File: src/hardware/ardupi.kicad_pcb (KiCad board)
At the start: 2 copper layers, 65 x 56 mm, 72 parts, among them J1 Conn_01x05, J2 Conn_01x06, J3 RPI-4B-Header, J4 PWM_Header, J5 Conn_01x02, J6 Conn_01x04, J7 Conn_01x04, J8 Conn_01x05, J9 Conn_01x10, M1 NEO-M8Q-01A, U1 ULN2803ADWR, U2 CAT24C32WI-GT3, U3 ADS1115IDGSR, U4 RFM95W-915S2, U5 MPU-9250, U6 PCA9685PW, U7 BMP280, U8 MPU-9250

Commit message: version bump
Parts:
- removed C_PCA1: 10uF, Capacitor_SMD:CP_Elec_8x5.4
- removed R1, R10, R5, R6, R8: 10k, Resistor_SMD:R_0402_1005Metric
- removed R16, R17, R18, R19, R20, R21, R22, R23: 220 Ω, Resistor_SMD:R_0402_1005Metric
- removed R2, R3, R4: 10K, Resistor_SMD:R_0402_1005Metric
- removed SJ1, SJ2, SJ3, SJ4, SJ5, SJ6: SolderJumper-Open_Pad, Ardupi:SolderJumper-Open_Pad
- removed U6: PCA9685PW, Ardupi:PCA9685PW
- removed U8: MPU-9250, Ardupi:MPU-9250
- J4: value PWM_Header -> Conn_01x06; footprint Ardupi:PWM_Header -> Connector_JST:JST_EH_B6B-EH-A_1x06_P2.50mm_Vertical
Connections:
- J4 pad 1: Net-(J4-Pad1) -> GND
- J4 pad 2: V_EXT -> /PCA_EN
- J4 pad 3: GND -> /SCL
- J4 pad 4: Net-(J4-Pad4) -> /SDA
- J4 pad 5: V_EXT -> +5V
- J4 pad 6: GND -> V_EXT

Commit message: update symbols
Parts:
- removed C4: 0.1uF, Capacitor_SMD:C_0402_1005Metric
- removed C6: 0.01uF, Capacitor_SMD:C_0402_1005Metric
- removed C8: 1uF, Capacitor_SMD:C_0402_1005Metric
- removed R24, R25, R31, R33, R34: 10KΩ, Resistor_SMD:R_0402_1005Metric
- removed U7: BMP280, Ardupi:BMP280
- added C12: 0.1uF, Capacitor_SMD:C_0402_1005Metric, F.Cu at (60.2, 140.2)
- added C14: 0.01uF, Capacitor_SMD:C_0402_1005Metric, F.Cu at (46.2, 153.8)
- added C15: 1uF, Capacitor_SMD:C_0402_1005Metric, F.Cu at (64.9, 134.3)
- added D1: B560C, Ardupi:B560C-13-F, F.Cu at (52.7, 137.1)
- added M2: NEO-M8Q-01A, Ardupi:NEO-M8Q-01A, F.Cu at (60.9, 118.6)
- added R1: 523k, Resistor_SMD:R_0402_1005Metric, F.Cu at (31.5, 163.7)
- added R10: 10KΩ, Resistor_SMD:R_0402_1005Metric, F.Cu at (57.3, 142.0)
- added R16: 10KΩ, Resistor_SMD:R_0402_1005Metric, F.Cu at (66.5, 128.3)
- added R17: 53.6 k, Resistor_SMD:R_0402_1005Metric, F.Cu at (47.1, 149.8)
- added R18: 10.2 k, Resistor_SMD:R_0402_1005Metric, F.Cu at (37.4, 154.0)
- added R2: 84.5, Resistor_SMD:R_0402_1005Metric, F.Cu at (66.5, 130.3)
- added R3: 162 k, Resistor_SMD:R_0402_1005Metric, F.Cu at (43.3, 153.2)
- added R4: 10KΩ, Resistor_SMD:R_0402_1005Metric, F.Cu at (47.1, 147.8)
- added R5: 10KΩ, Resistor_SMD:R_0402_1005Metric, F.Cu at (47.1, 126.1)
- added R6: 10KΩ, Resistor_SMD:R_0402_1005Metric, F.Cu at (59.1, 136.2)
- added R8: 13 k, Resistor_SMD:R_0402_1005Metric, F.Cu at (50.1, 126.1)
- added U6: BMP280, Ardupi:BMP280, F.Cu at (43.6, 148.3)
- J1: moved to F.Cu
- M1: value NEO-M8Q-01A -> RFM95W-915S2; footprint Ardupi:ublox_NEO -> Ardupi:RFM95W-915S2
- U1: value ULN2803ADWR -> CAT24C32WI-GT3; footprint Ardupi:ULN2803ADWR -> Ardupi:CAT24C32WI-GT3
- U2: value CAT24C32WI-GT3 -> ULN2803ADWR; footprint Ardupi:CAT24C32WI-GT3 -> Ardupi:ULN2803ADWR
- U4: value RFM95W-915S2 -> TPS54360BDDAR; footprint Ardupi:RFM95W-915S2 -> Ardupi:TPS54360BDDAR
- moved U5 100.5 mm to (43.1, 124.4)
- moved M1 84.4 mm to (44.1, 112.7)
- moved U1 81.2 mm to (37.3, 149.7)
- moved SJ7 79.6 mm to (47.9, 123.3)
- moved J1 78.4 mm to (72.1, 118.3), turned to 0 degrees
- moved C5 75.0 mm to (37.3, 163.6)
- moved R26 65.8 mm to (87.0, 110.8)
- moved C3 54.7 mm to (46.2, 151.8)
- moved R32 48.9 mm to (51.5, 122.5)
- moved R29 46.9 mm to (59.1, 134.2)
- moved U3 46.1 mm to (36.8, 123.8)
- moved R28 45.3 mm to (63.6, 128.3)
- moved R27 38.9 mm to (40.4, 154.0)
- moved C2 38.5 mm to (62.0, 136.3)
- moved C7 37.3 mm to (62.0, 134.3)
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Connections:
- M1 pad 10: GND -> unconnected-(M1-Pad10)
- M1 pad 12: GND -> unconnected-(M1-Pad12)
- M1 pad 13: GND -> unconnected-(M1-Pad13)
- U1 pad 1: /BUZZER -> GND
- U1 pad 2: /BUZZER -> GND
- U1 pad 3: /LED1 -> GND
- U1 pad 4: /LED1 -> GND
- U1 pad 5: /LED2 -> /ID_SD
- U1 pad 6: /LED2 -> /ID_SC
- U1 pad 7: /LED3 -> Net-(R11-Pad1)
- U1 pad 8: /LED3 -> +3V3
- U2 pad 1: GND -> /BUZZER
- U2 pad 2: GND -> /BUZZER
- U2 pad 3: GND -> /LED1
- U2 pad 4: GND -> /LED1
- U2 pad 5: /ID_SD -> /LED2
- U2 pad 6: /ID_SC -> /LED2
- U2 pad 7: Net-(R11-Pad1) -> /LED3
- U2 pad 8: +3V3 -> /LED3
- U4 pad 1: unconnected-(U4-Pad1) -> Net-(C8-Pad2)
- U4 pad 2: unconnected-(U4-Pad2) -> ESC_VIN
- U4 pad 3: unconnected-(U4-Pad3) -> Net-(R1-Pad2)
- U4 pad 4: unconnected-(U4-Pad4) -> Net-(R3-Pad1)
- U4 pad 5: unconnected-(U4-Pad5) -> FB
- U4 pad 6: unconnected-(U4-Pad6) -> Net-(C10-Pad1)
- U4 pad 7: unconnected-(U4-Pad7) -> Net-(C11-Pad1)
- U4 pad 8: unconnected-(U4-Pad8) -> Net-(C8-Pad1)
- U5 pad 13: +3V3 -> unconnected-(U5-Pad13)
- U5 pad 18: GND -> unconnected-(U5-Pad18)
- U5 pad 20: GND -> unconnected-(U5-Pad20)
- U5 pad 22: /SPI_CE0_N -> /SPI_CEO_N
- U5 pad 25: unconnected-(U5-Pad25) -> (no net)

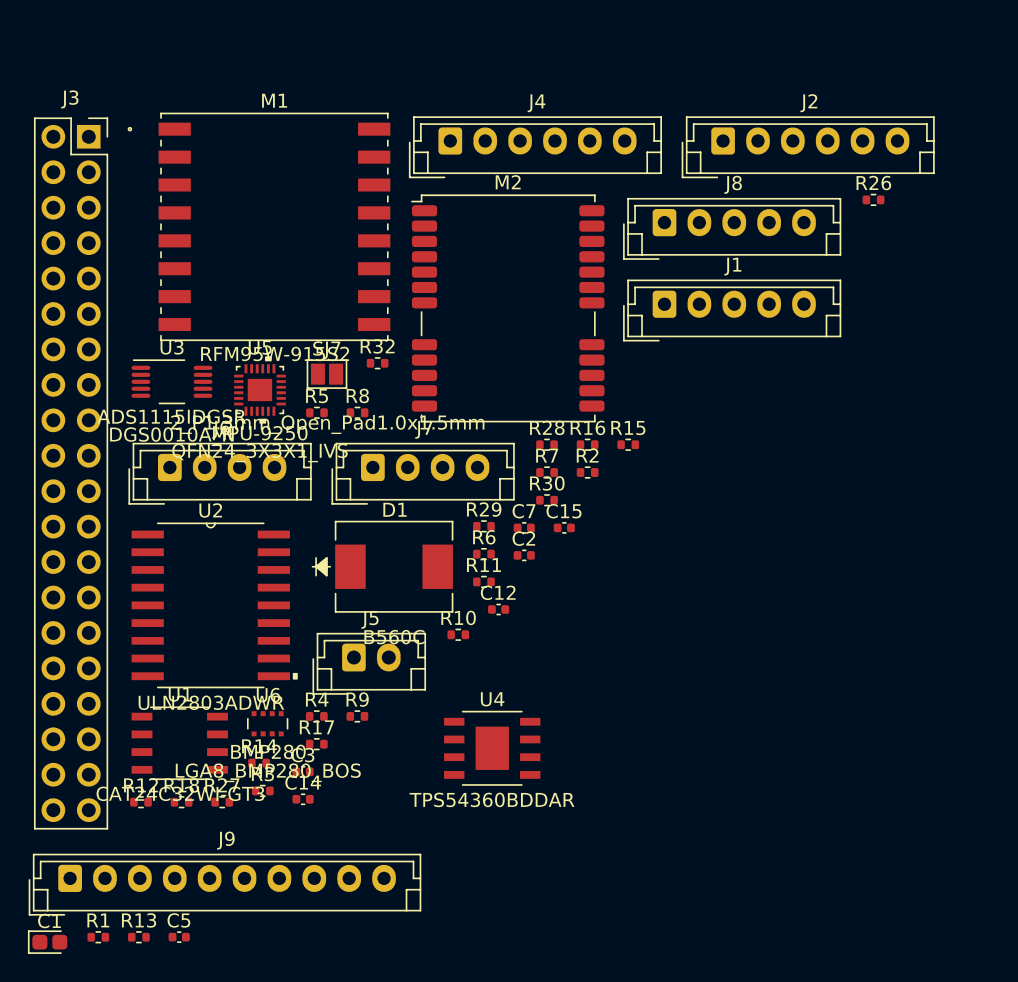
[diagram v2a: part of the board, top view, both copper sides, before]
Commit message: schematic fix and updates
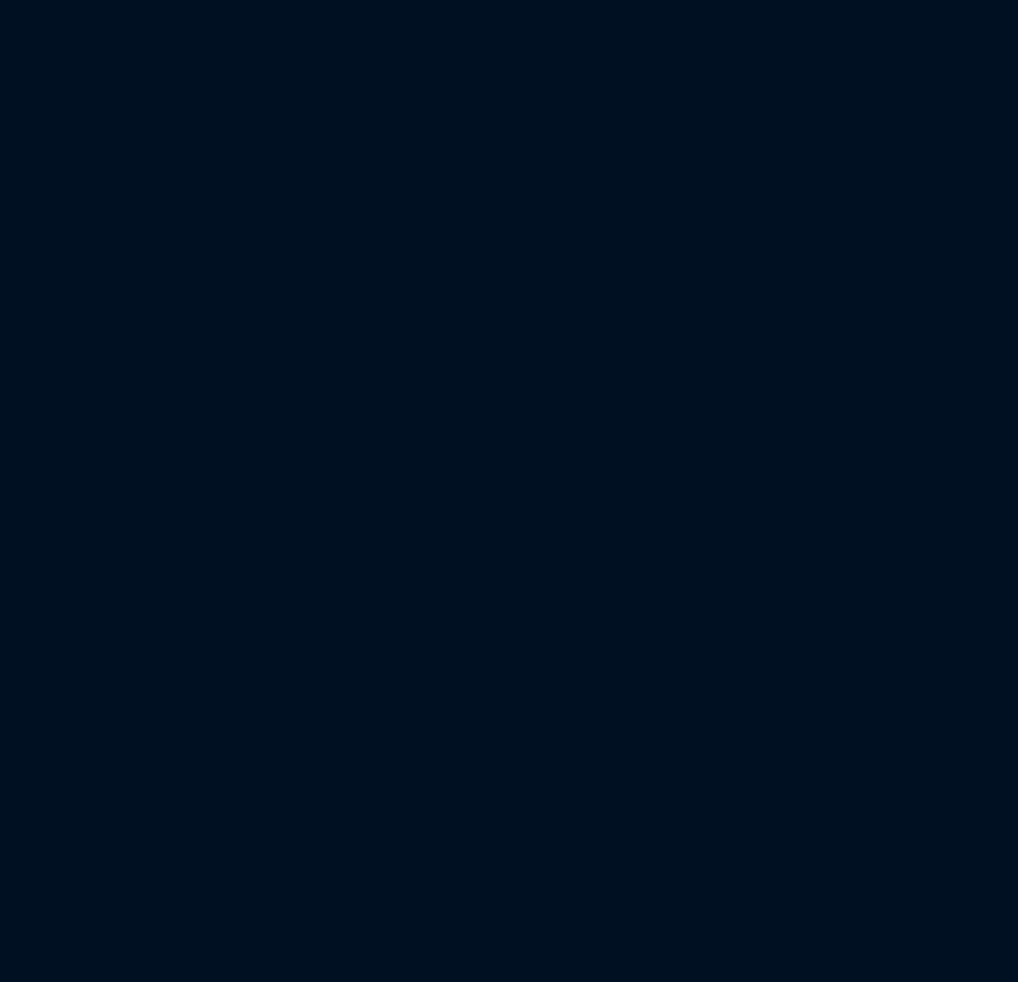
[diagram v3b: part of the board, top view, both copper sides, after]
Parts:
- removed C1: 100n, Capacitor_Tantalum_SMD:CP_EIA-1608-10_AVX-L
- removed C12, C5: 0.1uF, Capacitor_SMD:C_0402_1005Metric
- removed C14: 0.01uF, Capacitor_SMD:C_0402_1005Metric
- removed C15, C2, C7: 1uF, Capacitor_SMD:C_0402_1005Metric
- removed C3: 0.1uf, Capacitor_SMD:C_0402_1005Metric
- removed D1: B560C, Ardupi:B560C-13-F
- removed J1, J8: Conn_01x05, Connector_JST:JST_EH_B5B-EH-A_1x05_P2.50mm_Vertical
- removed J2, J4: Conn_01x06, Connector_JST:JST_EH_B6B-EH-A_1x06_P2.50mm_Vertical
- removed J3: RPI-4B-Header, Connector_PinSocket_2.54mm:PinSocket_2x20_P2.54mm_Vertical
- removed J5: Conn_01x02, Connector_JST:JST_EH_B2B-EH-A_1x02_P2.50mm_Vertical
- removed J6, J7: Conn_01x04, Connector_JST:JST_EH_B4B-EH-A_1x04_P2.50mm_Vertical
- removed J9: Conn_01x10, Connector_JST:JST_EH_B10B-EH-A_1x10_P2.50mm_Vertical
- removed M1: RFM95W-915S2, Ardupi:RFM95W-915S2
- removed M2: NEO-M8Q-01A, Ardupi:NEO-M8Q-01A
- removed R1: 523k, Resistor_SMD:R_0402_1005Metric
- removed R10, R14, R15, R16, R32, R4, R5, R6, R7, R9: 10KΩ, Resistor_SMD:R_0402_1005Metric
- removed R11: 1k, Resistor_SMD:R_0402_1005Metric
- removed R12, R13: 3.9k, Resistor_SMD:R_0402_1005Metric
- removed R17: 53.6 k, Resistor_SMD:R_0402_1005Metric
- removed R18: 10.2 k, Resistor_SMD:R_0402_1005Metric
- removed R2: 84.5, Resistor_SMD:R_0402_1005Metric
- removed R26: 10K, Resistor_SMD:R_0402_1005Metric
- removed R27: 460, Resistor_SMD:R_0402_1005Metric
- removed R28, R29, R30: 4.7KΩ, Resistor_SMD:R_0402_1005Metric
- removed R3: 162 k, Resistor_SMD:R_0402_1005Metric
- removed R8: 13 k, Resistor_SMD:R_0402_1005Metric
- removed SJ7: SolderJumper-Open_Pad, Ardupi:SolderJumper-Open_Pad
- removed U1: CAT24C32WI-GT3, Ardupi:CAT24C32WI-GT3
- removed U2: ULN2803ADWR, Ardupi:ULN2803ADWR
- removed U3: ADS1115IDGSR, Ardupi:ADS1115IDGSR
- removed U4: TPS54360BDDAR, Ardupi:TPS54360BDDAR
- removed U5: MPU-9250, Ardupi:MPU-9250
- removed U6: BMP280, Ardupi:BMP280

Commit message: schematic clean up, symbol updates.
+ pixhawk connector standards
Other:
- copper layers 2 -> 6
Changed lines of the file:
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@@
 (kicad_pcb (version 20211014) (generator pcbnew)
   (general
-    (thickness 1.6)
+    (thickness 1.89)
   )
   (paper "A4")
@@
   (layers
     (0 "F.Cu" signal)
+    (1 "In1.Cu" power)
+    (2 "In2.Cu" power)
+    (3 "In3.Cu" mixed)
+    (4 "In4.Cu" power)
     (31 "B.Cu" signal)
     (32 "B.Adhes" user "B.Adhesive")
@@
       (layer "F.Mask" (type "Top Solder Mask") (color "Green") (thickness 0.01))
       (layer "F.Cu" (type "copper") (thickness 0.035))
-      (layer "dielectric 1" (type "core") (thickness 1.51) (material "FR4") (epsilon_r 4.5) (loss_tangent 0.02))
+      (layer "dielectric 1" (type "prepreg") (thickness 0.1 locked) (material "2313") (epsilon_r 4.5) (loss_tangent 0.02))
+      (layer "In1.Cu" (type "copper") (thickness 0.0175))
+      (layer "dielectric 2" (type "core") (thickness 0.665 locked) (material "FR4") (epsilon_r 4.5) (loss_tangent 0.02))
+      (layer "In2.Cu" (type "copper") (thickness 0.0175))
+      (layer "dielectric 3" (type "prepreg") (thickness 0.2 locked) (material "2313") (epsilon_r 4.5) (loss_tangent 0.02))
+      (layer "In3.Cu" (type "copper") (thickness 0.0175))
+      (layer "dielectric 4" (type "core") (thickness 0.665 locked) (material "FR4") (epsilon_r 4.5) (loss_tangent 0.02))
+      (layer "In4.Cu" (type "copper") (thickness 0.0175))
+      (layer "dielectric 5" (type "prepreg") (thickness 0.1 locked) (material "2313*1") (epsilon_r 4.5) (loss_tangent 0.02))
       (layer "B.Cu" (type "copper") (thickness 0.035))
       (layer "B.Mask" (type "Bottom Solder Mask") (color "Green") (thickness 0.01))
       (layer "B.Paste" (type "Bottom Solder Paste"))
       (layer "B.SilkS" (type "Bottom Silk Screen"))
-      (copper_finish "None")
-      (dielectric_constraints no)
+      (copper_finish "User defined")
+      (dielectric_constraints yes)
     )
     (pad_to_mask_clearance 0)
